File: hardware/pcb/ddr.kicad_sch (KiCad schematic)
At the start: 26 parts, among them U2 MT41K256M16TW

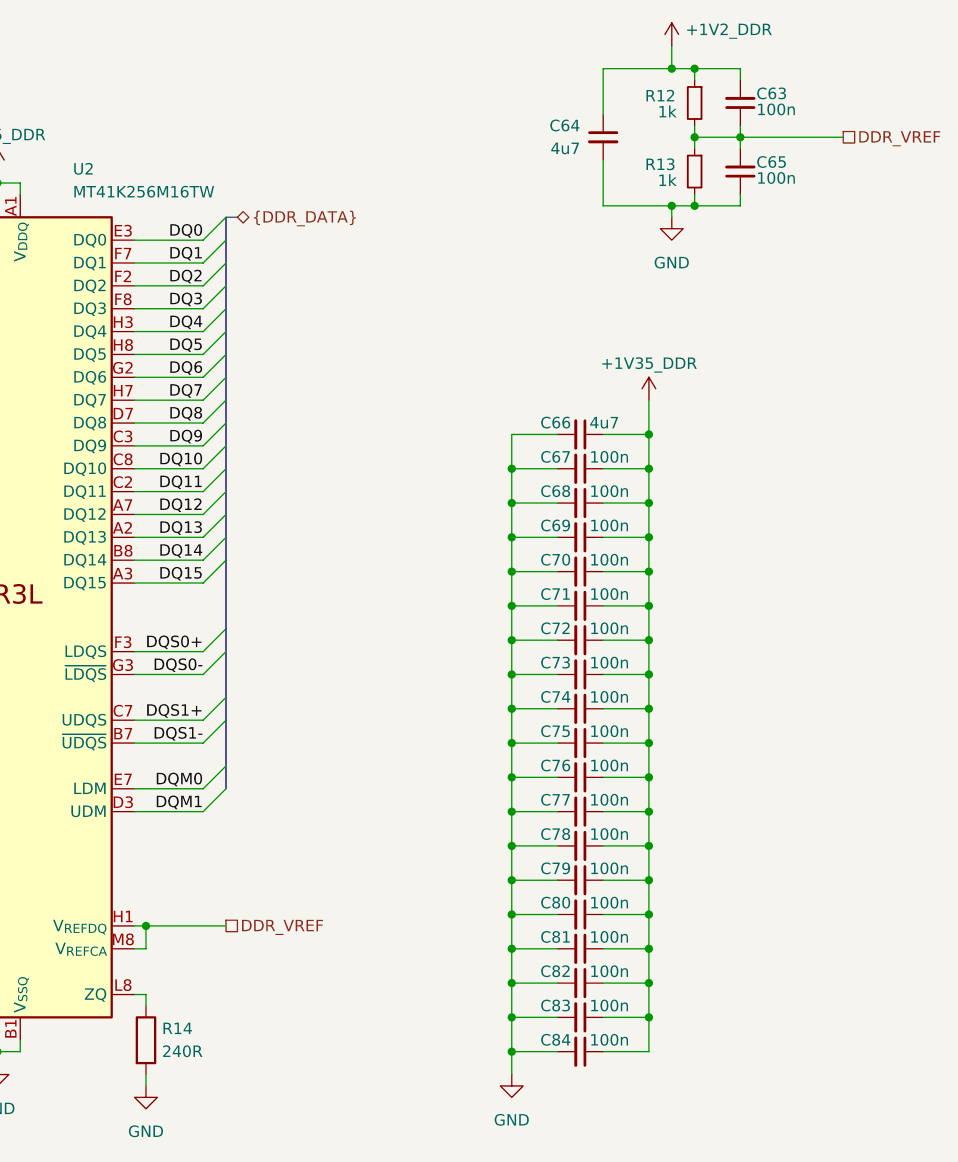
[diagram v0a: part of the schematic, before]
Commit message: removed testpoints on sd cards, since I can probe the pins there
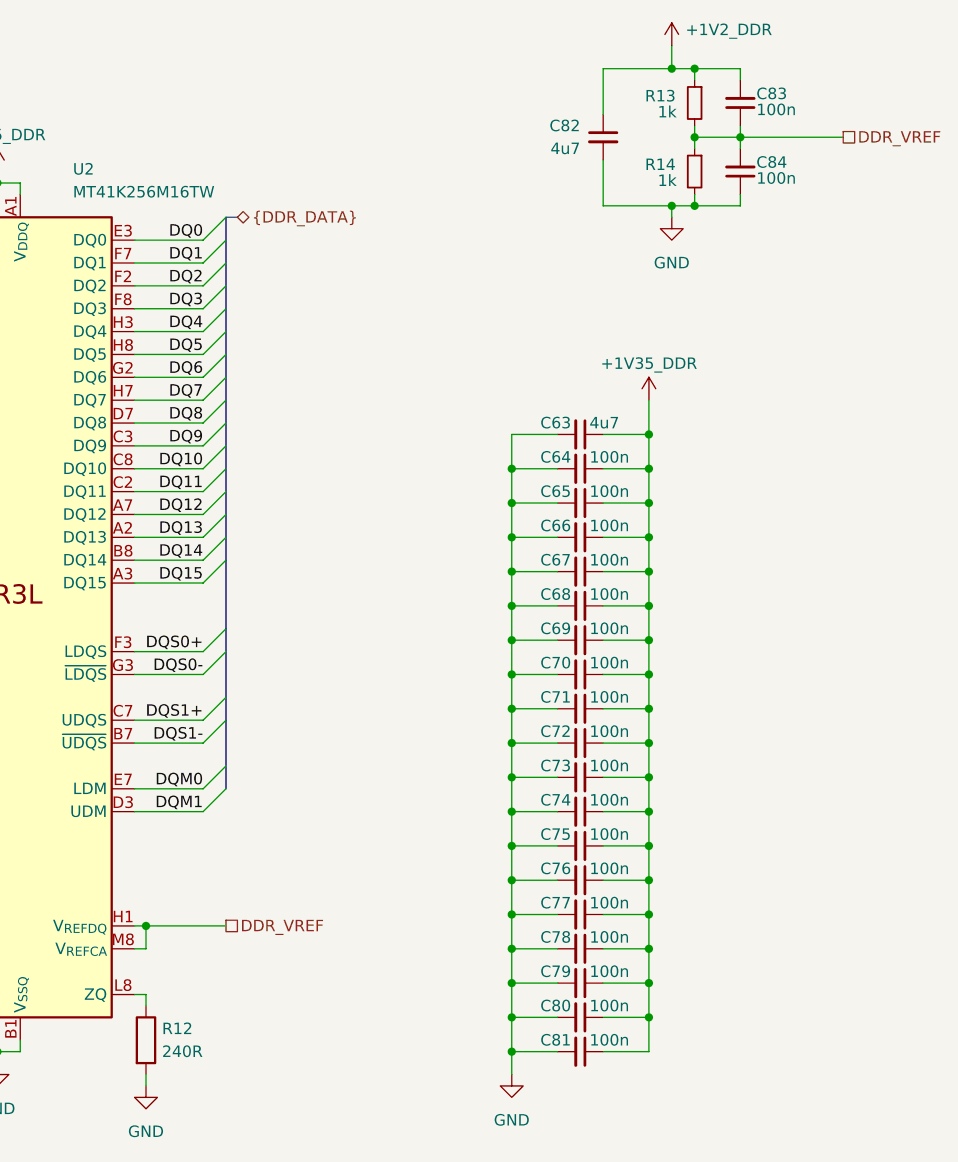
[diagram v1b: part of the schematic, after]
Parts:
- renumbered C66 to C63, C67 to C64, C68 to C65, C69 to C66, C70 to C67, C71 to C68, C72 to C69, C73 to C70, C74 to C71, C75 to C72, C76 to C73, C77 to C74, C78 to C75, C79 to C76, C80 to C77, C81 to C78, C82 to C79, C83 to C80, C84 to C81, C64 to C82, C63 to C83, C65 to C84, R14 to R12, R12 to R13, R13 to R14

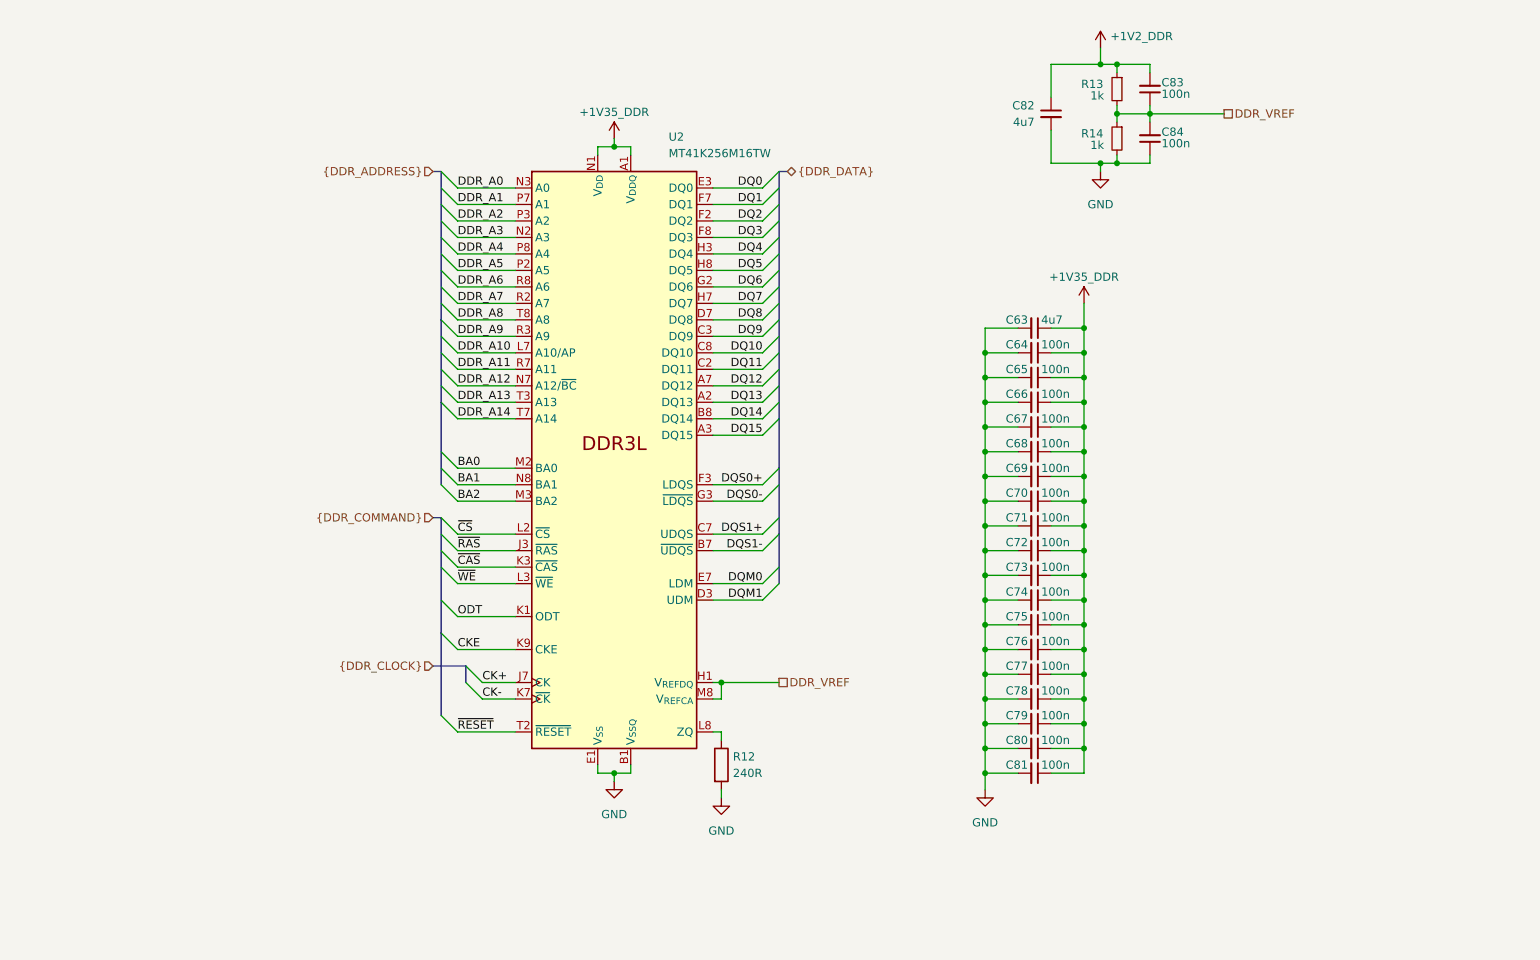
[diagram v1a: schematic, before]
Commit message: added terminatino and pull-up to ram
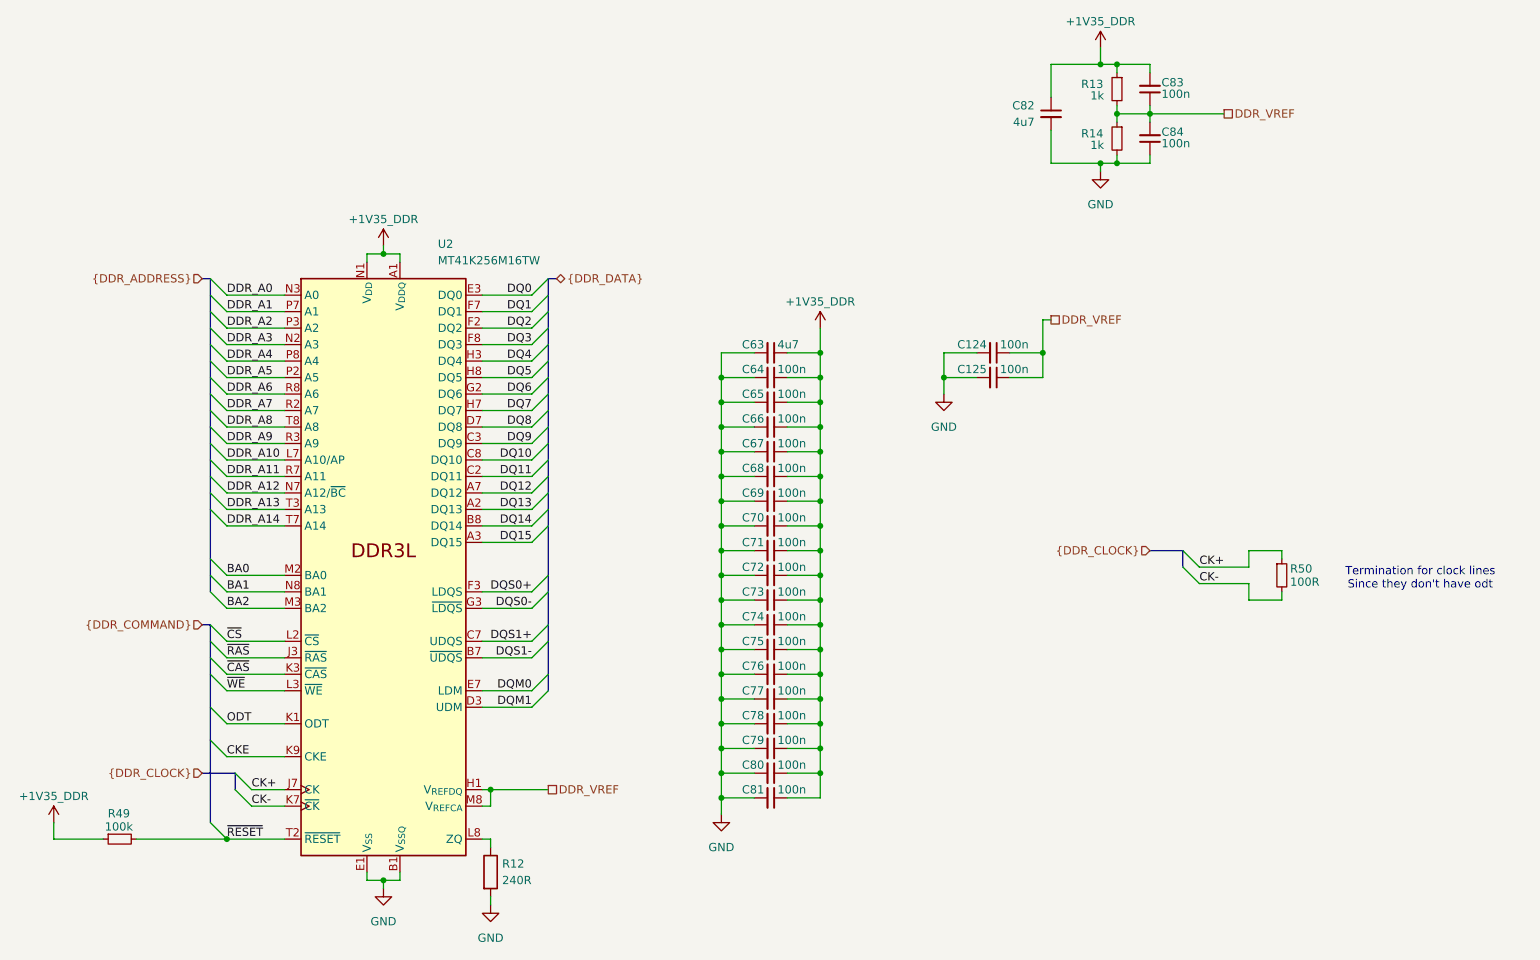
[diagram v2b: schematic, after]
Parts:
- added C124, C125: 100n, Capacitor_SMD:C_0402_1005Metric, symbol Device:C_Small
- added R49: 100k, Resistor_SMD:R_0402_1005Metric, symbol Device:R_Small
- added R50: 100R, Resistor_SMD:R_0402_1005Metric, symbol Device:R_Small
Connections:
- net +1V2_DDR is gone; now on net +1V35_DDR: C82.1, C83.2, R13.1
- net +1V35_DDR: now also R49.1
- net CK+: now also R50.1
- net CK-: now also R50.2
- net DDR_VREF: now also C124.1, C125.1
- net GND: now also C124.2, C125.2
- net ~{RESET}: now also R49.2
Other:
- note added: "Termination for clock lines Since they don't have odt"
- moved on the sheet: C63, C64, C65, C66, C67, C68, C69, C70, C71, C72, C73, C74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

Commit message: added capacitor to sama ddr vref pin
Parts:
- renumbered C124 to C82, C125 to C83, C82 to C84, C83 to C85, C84 to C86, R49 to R12, R12 to R13, R13 to R14, R14 to R15, R50 to R16
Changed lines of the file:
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@@
 		(in_pos_files yes)
 		(dnp no)
-		(property "Reference" "R12"
+		(property "Reference" "R13"
 			(at 102.108 146.05 0)
 			(show_name no)
@@
 			(project "meko"
 				(path "/da54f10a-146b-4941-a9c7-55c7173bb101/6a1996a1-d776-4235-b4ef-703258aa0c56"
-					(reference "R12")
+					(reference "R13")
 					(unit 1)
 				)
@@
 		(in_pos_files yes)
 		(dnp no)
-		(property "Reference" "#PWR043"
+		(property "Reference" "#PWR045"
 			(at 194.31 24.13 0)
 			(hide yes)
@@
 			(project "meko"
 				(path "/da54f10a-146b-4941-a9c7-55c7173bb101/6a1996a1-d776-4235-b4ef-703258aa0c56"
-					(reference "#PWR043")
+					(reference "#PWR045")
 					(unit 1)
 				)
@@
 		(in_pos_files yes)
 		(dnp no)
-		(property "Reference" "C124"
+		(property "Reference" "C82"
 			(at 176.784 66.04 90)
 			(show_name no)
@@
 			(project "meko"
 				(path "/da54f10a-146b-4941-a9c7-55c7173bb101/6a1996a1-d776-4235-b4ef-703258aa0c56"
-					(reference "C124")
+					(reference "C82")
 					(unit 1)
 				)
@@
 		(in_pos_files yes)
 		(dnp no)
-		(property "Reference" "R50"
+		(property "Reference" "R16"
 			(at 223.52 100.584 0)
 			(show_name no)
@@
 			(project "meko"
 				(path "/da54f10a-146b-4941-a9c7-55c7173bb101/6a1996a1-d776-4235-b4ef-703258aa0c56"
-					(reference "R50")
+					(reference "R16")
 					(unit 1)
 				)
@@
 		(dnp no)
 		(fields_autoplaced yes)
-		(property "Reference" "#PWR039"
+		(property "Reference" "#PWR040"
 			(at 83.82 156.21 0)
 			(hide yes)
@@
 			(project "meko"
 				(path "/da54f10a-146b-4941-a9c7-55c7173bb101/6a1996a1-d776-4235-b4ef-703258aa0c56"
-					(reference "#PWR039")
+					(reference "#PWR040")
 					(unit 1)
 				)
@@
 		(dnp no)
 		(fields_autoplaced yes)
-		(property "Reference" "#PWR041"
+		(property "Reference" "#PWR042"
 			(at 135.89 144.78 0)
 			(hide yes)
@@
 			(project "meko"
 				(path "/da54f10a-146b-4941-a9c7-55c7173bb101/6a1996a1-d776-4235-b4ef-703258aa0c56"
-					(reference "#PWR041")
+					(reference "#PWR042")
 					(unit 1)
 				)
@@
 		(in_pos_files yes)
 		(dnp no)
-		(property "Reference" "#PWR038"
+		(property "Reference" "#PWR039"
 			(at 83.82 54.61 0)
 			(hide yes)
@@
 			(project "meko"
 				(path "/da54f10a-146b-4941-a9c7-55c7173bb101/6a1996a1-d776-4235-b4ef-703258aa0c56"
-					(reference "#PWR038")
+					(reference "#PWR039")
 					(unit 1)
 				)
@@
 		(in_pos_files yes)
 		(dnp no)
-		(property "Reference" "C83"
+		(property "Reference" "C85"
 			(at 203.708 25.654 0)
 			(show_name no)
@@
 			(project "meko"
 				(path "/da54f10a-146b-4941-a9c7-55c7173bb101/6a1996a1-d776-4235-b4ef-703258aa0c56"
-					(reference "C83")
+					(reference "C85")
 					(unit 1)
 				)
@@
 		(in_pos_files yes)
 		(dnp no)
-		(property "Reference" "R13"
+		(property "Reference" "R14"
 			(at 193.04 25.908 0)
 			(show_name no)
@@
 			(project "meko"
 				(path "/da54f10a-146b-4941-a9c7-55c7173bb101/6a1996a1-d776-4235-b4ef-703258aa0c56"
-					(reference "R13")
+					(reference "R14")
 					(unit 1)
 				)
@@
 		(in_pos_files yes)
 		(dnp no)
-		(property "Reference" "R49"
+		(property "Reference" "R12"
 			(at 43.053 138.303 90)
 			(show_name no)
@@
 			(project "meko"
 				(path "/da54f10a-146b-4941-a9c7-55c7173bb101/6a1996a1-d776-4235-b4ef-703258aa0c56"
-					(reference "R49")
+					(reference "R12")
 					(unit 1)
 				)
@@
 		(in_pos_files yes)
 		(dnp no)
-		(property "Reference" "#PWR0139"
+		(property "Reference" "#PWR038"
 			(at 33.02 143.51 0)
 			(hide yes)
@@
 			(project "meko"
 				(path "/da54f10a-146b-4941-a9c7-55c7173bb101/6a1996a1-d776-4235-b4ef-703258aa0c56"
-					(reference "#PWR0139")
+					(reference "#PWR038")
 					(unit 1)
 				)
@@
 		(dnp no)
 		(fields_autoplaced yes)
-		(property "Reference" "#PWR044"
+		(property "Reference" "#PWR046"
 			(at 194.31 45.72 0)
 			(hide yes)
@@
 			(project "meko"
 				(path "/da54f10a-146b-4941-a9c7-55c7173bb101/6a1996a1-d776-4235-b4ef-703258aa0c56"
-					(reference "#PWR044")
+					(reference "#PWR046")
 					(unit 1)
 				)
@@
 		(in_pos_files yes)
 		(dnp no)
-		(property "Reference" "C84"
+		(property "Reference" "C86"
 			(at 203.708 33.274 0)
 			(show_name no)
@@
 			(project "meko"
 				(path "/da54f10a-146b-4941-a9c7-55c7173bb101/6a1996a1-d776-4235-b4ef-703258aa0c56"
-					(reference "C84")
+					(reference "C86")
 					(unit 1)
 				)
@@
 		(in_pos_files yes)
 		(dnp no)
-		(property "Reference" "#PWR042"
+		(property "Reference" "#PWR043"
 			(at 151.13 67.31 0)
 			(hide yes)
@@
 			(project "meko"
 				(path "/da54f10a-146b-4941-a9c7-55c7173bb101/6a1996a1-d776-4235-b4ef-703258aa0c56"
-					(reference "#PWR042")
+					(reference "#PWR043")
 					(unit 1)
 				)
@@
 		(dnp no)
 		(fields_autoplaced yes)
-		(property "Reference" "#PWR0138"
+		(property "Reference" "#PWR044"
 			(at 170.18 80.01 0)
 			(hide yes)
@@
 			(project "meko"
 				(path "/da54f10a-146b-4941-a9c7-55c7173bb101/6a1996a1-d776-4235-b4ef-703258aa0c56"
-					(reference "#PWR0138")
+					(reference "#PWR044")
 					(unit 1)
 				)
@@
 		(dnp no)
 		(fields_autoplaced yes)
-		(property "Reference" "#PWR040"
+		(property "Reference" "#PWR041"
 			(at 100.33 158.75 0)
 			(hide yes)
@@
 			(project "meko"
 				(path "/da54f10a-146b-4941-a9c7-55c7173bb101/6a1996a1-d776-4235-b4ef-703258aa0c56"
-					(reference "#PWR040")
+					(reference "#PWR041")
 					(unit 1)
 				)
@@
 		(in_pos_files yes)
 		(dnp no)
-		(property "Reference" "R14"
+		(property "Reference" "R15"
 			(at 193.04 33.528 0)
 			(show_name no)
@@
 			(project "meko"
 				(path "/da54f10a-146b-4941-a9c7-55c7173bb101/6a1996a1-d776-4235-b4ef-703258aa0c56"
-					(reference "R14")
+					(reference "R15")
 					(unit 1)
 				)
@@
 		(in_pos_files yes)
 		(dnp no)
-		(property "Reference" "C125"
+		(property "Reference" "C83"
 			(at 176.784 69.85 90)
 			(show_name no)
@@
 			(project "meko"
 				(path "/da54f10a-146b-4941-a9c7-55c7173bb101/6a1996a1-d776-4235-b4ef-703258aa0c56"
-					(reference "C125")
+					(reference "C83")
 					(unit 1)
 				)
@@
 		(in_pos_files yes)
 		(dnp no)
-		(property "Reference" "C82"
+		(property "Reference" "C84"
 			(at 184.15 29.2162 0)
 			(show_name no)
@@
 			(project "meko"
 				(path "/da54f10a-146b-4941-a9c7-55c7173bb101/6a1996a1-d776-4235-b4ef-703258aa0c56"
-					(reference "C82")
+					(reference "C84")
 					(unit 1)
 				)

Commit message: didn't save last time :sob:
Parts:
- renumbered C63 to C64, C64 to C65, C65 to C66, C66 to C67, C67 to C68, C68 to C69, C69 to C70, C70 to C71, C71 to C72, C72 to C73, C73 to C74, C74 to C75, C75 to C76, C76 to C77, C77 to C78, C78 to C79, C79 to C80, C80 to C81, C81 to C82, C82 to C83, C83 to C84, C84 to C85, C85 to C86, C86 to C87

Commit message: added pullups for jtag
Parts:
- renumbered C86 to C64, C85 to C65, C87 to C66, C64 to C67, C83 to C68, C65 to C69, C84 to C70, C66 to C71, C67 to C72, C68 to C73, C69 to C74, C70 to C75, C71 to C76, C72 to C77, C73 to C78, C74 to C79, C75 to C80, C76 to C81, C77 to C82, C78 to C83, C79 to C84, C80 to C85, C81 to C86, C82 to C87, R14 to R15, R15 to R16, R16 to R17, R12 to R18, R13 to R19

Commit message: moved some caps to 0201
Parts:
- C64, C66, C68, C69, C70, C71, C72, C73, C74, C75, C76, C77, C78, C79, C80, C81, C82, C83, C84, C85, C86, C87: footprint Capacitor_SMD:C_0402_1005Metric -> Capacitor_SMD:C_0201_0603Metric
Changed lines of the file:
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@@
 			)
 		)
-		(property "Footprint" "Capacitor_SMD:C_0402_1005Metric"
+		(property "Footprint" "Capacitor_SMD:C_0201_0603Metric"
 			(at 143.51 113.03 0)
 			(hide yes)
@@
 			)
 		)
-		(property "Footprint" "Capacitor_SMD:C_0402_1005Metric"
+		(property "Footprint" "Capacitor_SMD:C_0201_0603Metric"
 			(at 143.51 86.36 0)
 			(hide yes)
@@
 			)
 		)
-		(property "Footprint" "Capacitor_SMD:C_0402_1005Metric"
+		(property "Footprint" "Capacitor_SMD:C_0201_0603Metric"
 			(at 143.51 93.98 0)
 			(hide yes)
@@
 			)
 		)
-		(property "Footprint" "Capacitor_SMD:C_0402_1005Metric"
+		(property "Footprint" "Capacitor_SMD:C_0201_0603Metric"
 			(at 143.51 90.17 0)
 			(hide yes)
@@
 			)
 		)
-		(property "Footprint" "Capacitor_SMD:C_0402_1005Metric"
+		(property "Footprint" "Capacitor_SMD:C_0201_0603Metric"
 			(at 143.51 120.65 0)
 			(hide yes)
@@
 			)
 		)
-		(property "Footprint" "Capacitor_SMD:C_0402_1005Metric"
+		(property "Footprint" "Capacitor_SMD:C_0201_0603Metric"
 			(at 177.8 67.31 0)
 			(hide yes)
@@
 			)
 		)
-		(property "Footprint" "Capacitor_SMD:C_0402_1005Metric"
+		(property "Footprint" "Capacitor_SMD:C_0201_0603Metric"
 			(at 143.51 124.46 0)
 			(hide yes)
@@
 			)
 		)
-		(property "Footprint" "Capacitor_SMD:C_0402_1005Metric"
+		(property "Footprint" "Capacitor_SMD:C_0201_0603Metric"
 			(at 143.51 71.12 0)
 			(hide yes)
@@
 			)
 		)
-		(property "Footprint" "Capacitor_SMD:C_0402_1005Metric"
+		(property "Footprint" "Capacitor_SMD:C_0201_0603Metric"
 			(at 143.51 128.27 0)
 			(hide yes)
@@
 			)
 		)
-		(property "Footprint" "Capacitor_SMD:C_0402_1005Metric"
+		(property "Footprint" "Capacitor_SMD:C_0201_0603Metric"
 			(at 143.51 82.55 0)
 			(hide yes)
@@
 			)
 		)
-		(property "Footprint" "Capacitor_SMD:C_0402_1005Metric"
+		(property "Footprint" "Capacitor_SMD:C_0201_0603Metric"
 			(at 143.51 132.08 0)
 			(hide yes)
@@
 			)
 		)
-		(property "Footprint" "Capacitor_SMD:C_0402_1005Metric"
+		(property "Footprint" "Capacitor_SMD:C_0201_0603Metric"
 			(at 201.93 26.67 0)
 			(hide yes)
@@
 			)
 		)
-		(property "Footprint" "Capacitor_SMD:C_0402_1005Metric"
+		(property "Footprint" "Capacitor_SMD:C_0201_0603Metric"
 			(at 143.51 109.22 0)
 			(hide yes)
@@
 			)
 		)
-		(property "Footprint" "Capacitor_SMD:C_0402_1005Metric"
+		(property "Footprint" "Capacitor_SMD:C_0201_0603Metric"
 			(at 143.51 78.74 0)
 			(hide yes)
@@
 			)
 		)
-		(property "Footprint" "Capacitor_SMD:C_0402_1005Metric"
+		(property "Footprint" "Capacitor_SMD:C_0201_0603Metric"
 			(at 143.51 97.79 0)
 			(hide yes)
@@
 			)
 		)
-		(property "Footprint" "Capacitor_SMD:C_0402_1005Metric"
+		(property "Footprint" "Capacitor_SMD:C_0201_0603Metric"
 			(at 143.51 116.84 0)
 			(hide yes)
@@
 			)
 		)
-		(property "Footprint" "Capacitor_SMD:C_0402_1005Metric"
+		(property "Footprint" "Capacitor_SMD:C_0201_0603Metric"
 			(at 143.51 135.89 0)
 			(hide yes)
@@
 			)
 		)
-		(property "Footprint" "Capacitor_SMD:C_0402_1005Metric"
+		(property "Footprint" "Capacitor_SMD:C_0201_0603Metric"
 			(at 143.51 74.93 0)
 			(hide yes)
@@
 			)
 		)
-		(property "Footprint" "Capacitor_SMD:C_0402_1005Metric"
+		(property "Footprint" "Capacitor_SMD:C_0201_0603Metric"
 			(at 143.51 105.41 0)
 			(hide yes)
@@
 			)
 		)
-		(property "Footprint" "Capacitor_SMD:C_0402_1005Metric"
+		(property "Footprint" "Capacitor_SMD:C_0201_0603Metric"
 			(at 201.93 34.29 0)
 			(hide yes)
@@
 			)
 		)
-		(property "Footprint" "Capacitor_SMD:C_0402_1005Metric"
+		(property "Footprint" "Capacitor_SMD:C_0201_0603Metric"
 			(at 177.8 71.12 0)
 			(hide yes)
@@
 			)
 		)
-		(property "Footprint" "Capacitor_SMD:C_0402_1005Metric"
+		(property "Footprint" "Capacitor_SMD:C_0201_0603Metric"
 			(at 143.51 101.6 0)
 			(hide yes)

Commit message: vendored in a bunch of footprints
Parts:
- U2: footprint Package_BGA:Micron_FBGA-96_8x14mm_Layout9x16_P0.8mm -> MT41K256M16TW:Micron_FBGA-96_8x14mm_Layout9x16_P0.8mm
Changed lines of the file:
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@@
 			)
 		)
-		(property "Footprint" "Package_BGA:Micron_FBGA-96_8x14mm_Layout9x16_P0.8mm"
+		(property "Footprint" "MT41K256M16TW:Micron_FBGA-96_8x14mm_Layout9x16_P0.8mm"
 			(at 83.82 155.194 0)
 			(hide yes)
